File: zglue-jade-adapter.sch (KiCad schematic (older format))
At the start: 63 parts, among them J1 543630489, J2 543630489, U1 zGlue-Jade

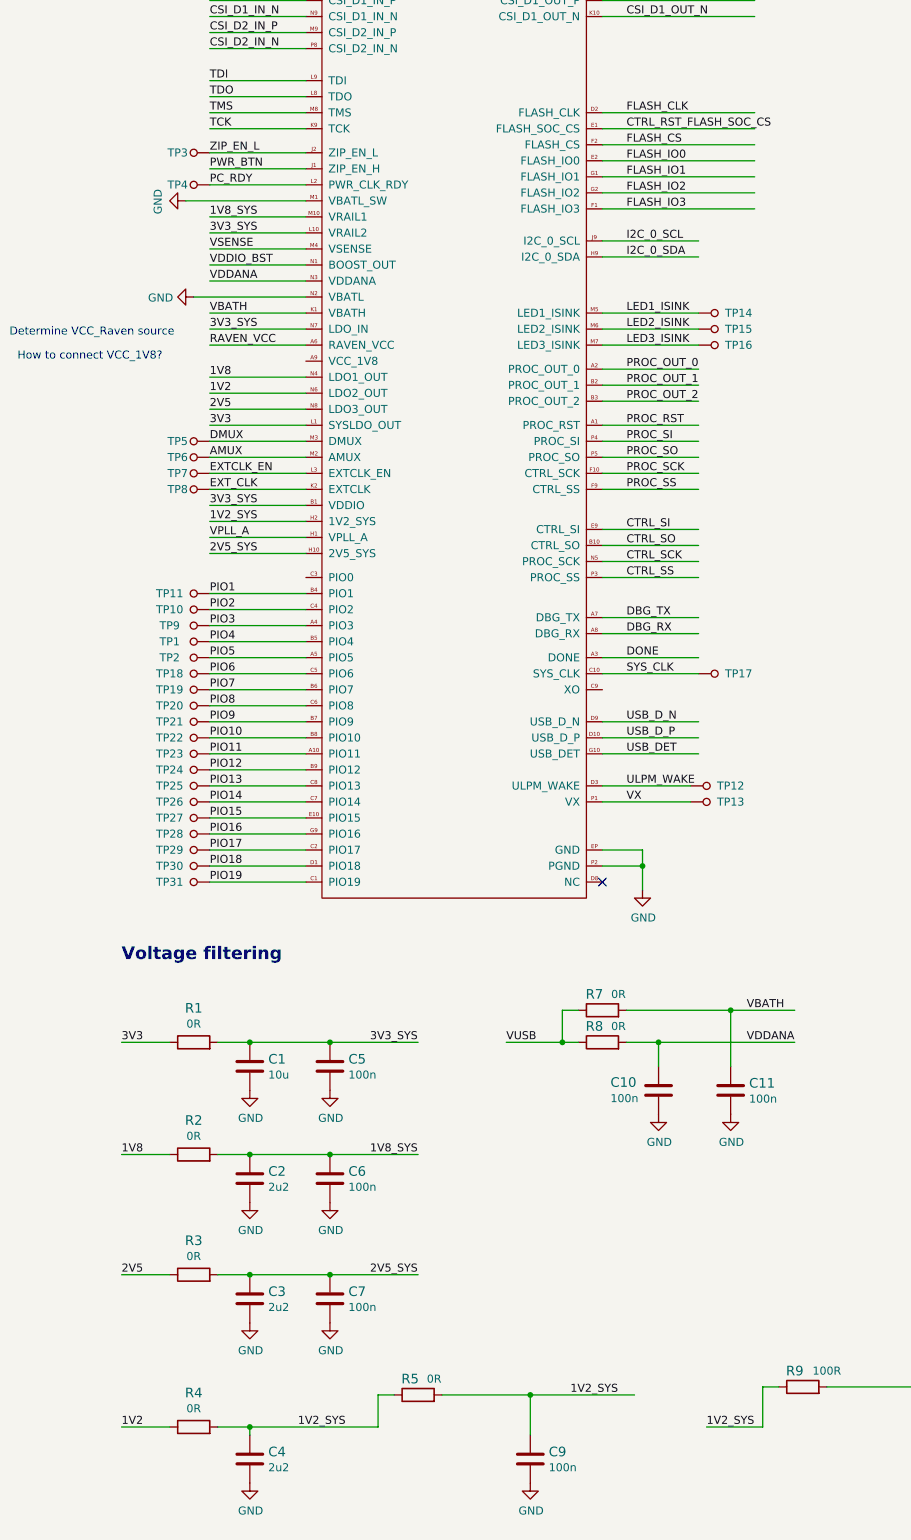
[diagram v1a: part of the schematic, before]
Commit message: Move C1,2,3,4 closer to LDOs' outputs
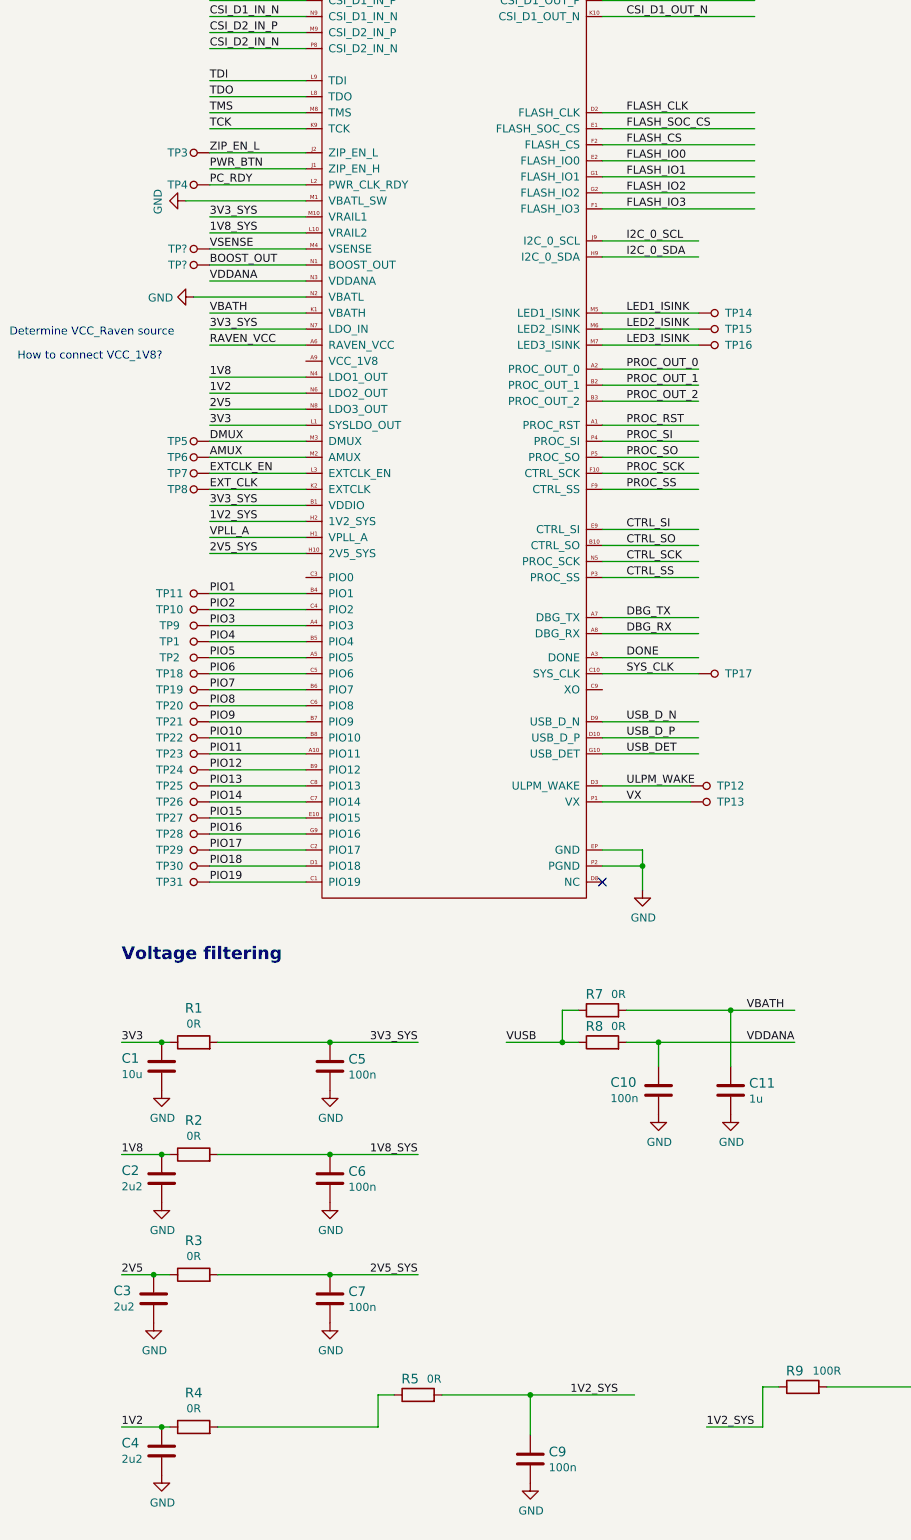
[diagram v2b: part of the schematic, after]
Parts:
- removed C11: C_100n_0402_6V3, antmicro-footprints:0402-cap, symbol antmicroCapacitors0402:C_100n_0402_6V3
- added C11: C_1u_0603, antmicro-footprints:0603-cap, symbol antmicroCapacitors0603:C_1u_0603
- added TP? (x2): TP_SMD1MM, antmicro-footprints:Testpoint_smd_1mm, symbol antmicroTestPoints:TP_SMD1MM
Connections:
- net labels added: BOOST_OUT, FLASH_SOC_CS
- net labels removed: VDDIO_BST
- wire segments 249 -> 248
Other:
- moved on the sheet: C1, C2, C3, C4
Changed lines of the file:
@@
 Wire Wire Line
 	2350 3000 1750 3000
+Text Label 1750 3000 0    50   ~ 0
+1V8_SYS
 Text Label 1750 2900 0    50   ~ 0
-1V8_SYS
-Text Label 1750 3000 0    50   ~ 0
 3V3_SYS
 Wire Wire Line
@@
 VSENSE
 Text Label 1750 3200 0    50   ~ 0
-VDDIO_BST
+BOOST_OUT
 Text Label 1750 5450 0    50   ~ 0
 PIO3
@@
 Jade chip
 $Comp
-L antmicroCapacitors0402:C_10u_0402 C1
-U 1 1 5DA0000B
-P 2000 8200
-F 0 "C1" H 2115 8245 60  0000 L CNN
-F 1 "C_10u_0402" H 2000 8050 60  0001 C CNN
-F 2 "antmicro-footprints:0402-cap" H 2200 8400 60  0001 L CNN
-F 3 "" H 2000 8200 50  0001 C CNN
-F 4 "TDK" H 2200 8600 60  0001 L CNN "Manufacturer"
-F 5 "C1005X5R0J106M050BC" H 2200 8500 60  0001 L CNN "MPN"
-F 6 "10u" H 2115 8147 50  0000 L CNN "Val"
-	1    2000 8200
-	1    0    0    -1
-$EndComp
-$Comp
 L antmicroCapacitors0402:C_100n_0402_6V3 C5
 U 1 1 5DA00317
@@
 L power:GND #PWR03
 U 1 1 5DA0044B
-P 2000 8350
-F 0 "#PWR03" H 2000 8100 50  0001 C CNN
-F 1 "GND" H 2005 8177 50  0000 C CNN
-F 2 "" H 2000 8350 50  0001 C CNN
-F 3 "" H 2000 8350 50  0001 C CNN
-	1    2000 8350
+P 1450 8350
+F 0 "#PWR03" H 1450 8100 50  0001 C CNN
+F 1 "GND" H 1455 8177 50  0000 C CNN
+F 2 "" H 1450 8350 50  0001 C CNN
+F 3 "" H 1450 8350 50  0001 C CNN
+	1    1450 8350
 	1    0    0    -1
 $EndComp
@@
 $EndComp
 Wire Wire Line
-	1800 8050 2000 8050
-Connection ~ 2000 8050
-Wire Wire Line
-	2000 8050 2500 8050
-Wire Wire Line
 	2500 8050 3050 8050
 Connection ~ 2500 8050
 Wire Wire Line
-	1500 8050 1200 8050
+	1500 8050 1450 8050
 Text Label 1200 8050 0    50   ~ 0
 3V3
@@
 L power:GND #PWR04
 U 1 1 5DA29CC6
-P 2000 9050
-F 0 "#PWR04" H 2000 8800 50  0001 C CNN
-F 1 "GND" H 2005 8877 50  0000 C CNN
-F 2 "" H 2000 9050 50  0001 C CNN
-F 3 "" H 2000 9050 50  0001 C CNN
-	1    2000 9050
+P 1450 9050
+F 0 "#PWR04" H 1450 8800 50  0001 C CNN
+F 1 "GND" H 1455 8877 50  0000 C CNN
+F 2 "" H 1450 9050 50  0001 C CNN
+F 3 "" H 1450 9050 50  0001 C CNN
+	1    1450 9050
 	1    0    0    -1
 $EndComp
@@
 Connection ~ 2500 8750
 Wire Wire Line
-	1500 8750 1200 8750
-Wire Wire Line
-	1800 8750 2000 8750
+	1500 8750 1450 8750
 $Comp
 L antmicroCapacitors0402:C_2u2_0402 C2
 U 1 1 5DA30683
-P 2000 8900
-F 0 "C2" H 2115 8945 60  0000 L CNN
-F 1 "C_2u2_0402" H 2000 8750 60  0001 C CNN
-F 2 "antmicro-footprints:0402-cap" H 2200 9100 60  0001 L CNN
-F 3 "" H 2000 8900 50  0001 C CNN
-F 4 "TDK" H 2200 9300 60  0001 L CNN "Manufacturer"
-F 5 "C1005X5R1A225K050BC" H 2200 9200 60  0001 L CNN "MPN"
-F 6 "2u2" H 2115 8847 50  0000 L CNN "Val"
-	1    2000 8900
-	1    0    0    -1
-$EndComp
-Connection ~ 2000 8750
-Wire Wire Line
-	2000 8750 2500 8750
+P 1450 8900
+F 0 "C2" H 1200 8950 60  0000 L CNN
+F 1 "C_2u2_0402" H 1450 8750 60  0001 C CNN
+F 2 "antmicro-footprints:0402-cap" H 1650 9100 60  0001 L CNN
+F 3 "" H 1450 8900 50  0001 C CNN
+F 4 "TDK" H 1650 9300 60  0001 L CNN "Manufacturer"
+F 5 "C1005X5R1A225K050BC" H 1650 9200 60  0001 L CNN "MPN"
+F 6 "2u2" H 1200 8850 50  0000 L CNN "Val"
+	1    1450 8900
+	1    0    0    -1
+$EndComp
 $Comp
 L power:GND #PWR06
 U 1 1 5DA307EF
-P 2000 10800
-F 0 "#PWR06" H 2000 10550 50  0001 C CNN
-F 1 "GND" H 2005 10627 50  0000 C CNN
-F 2 "" H 2000 10800 50  0001 C CNN
-F 3 "" H 2000 10800 50  0001 C CNN
-	1    2000 10800
+P 1450 10750
+F 0 "#PWR06" H 1450 10500 50  0001 C CNN
+F 1 "GND" H 1455 10577 50  0000 C CNN
+F 2 "" H 1450 10750 50  0001 C CNN
+F 3 "" H 1450 10750 50  0001 C CNN
+	1    1450 10750
 	1    0    0    -1
 $EndComp
@@
 $EndComp
 Wire Wire Line
-	1500 10450 1200 10450
-Wire Wire Line
-	1800 10450 2000 10450
-Connection ~ 2000 10450
+	1500 10450 1450 10450
 $Comp
 L antmicroCapacitors0402:C_2u2_0402 C4
 U 1 1 5DA3080C
-P 2000 10650
-F 0 "C4" H 2115 10695 60  0000 L CNN
-F 1 "C_2u2_0402" H 2000 10500 60  0001 C CNN
-F 2 "antmicro-footprints:0402-cap" H 2200 10850 60  0001 L CNN
-F 3 "" H 2000 10650 50  0001 C CNN
-F 4 "TDK" H 2200 11050 60  0001 L CNN "Manufacturer"
-F 5 "C1005X5R1A225K050BC" H 2200 10950 60  0001 L CNN "MPN"
-F 6 "2u2" H 2115 10597 50  0000 L CNN "Val"
-	1    2000 10650
+P 1450 10600
+F 0 "C4" H 1200 10650 60  0000 L CNN
+F 1 "C_2u2_0402" H 1450 10450 60  0001 C CNN
+F 2 "antmicro-footprints:0402-cap" H 1650 10800 60  0001 L CNN
+F 3 "" H 1450 10600 50  0001 C CNN
+F 4 "TDK" H 1650 11000 60  0001 L CNN "Manufacturer"
+F 5 "C1005X5R1A225K050BC" H 1650 10900 60  0001 L CNN "MPN"
+F 6 "2u2" H 1200 10550 50  0000 L CNN "Val"
+	1    1450 10600
 	1    0    0    -1
 $EndComp
@@
 Wire Wire Line
 	2800 10250 2800 10450
-Text Label 2300 10450 0    50   ~ 0
-1V2_SYS
-Wire Wire Line
-	2000 10450 2800 10450
-Wire Wire Line
-	2000 10500 2000 10450
 Wire Wire Line
 	2900 10250 2800 10250
@@
 L power:GND #PWR05
 U 1 1 5DB84A7E
-P 2000 9800
-F 0 "#PWR05" H 2000 9550 50  0001 C CNN
-F 1 "GND" H 2005 9627 50  0000 C CNN
-F 2 "" H 2000 9800 50  0001 C CNN
-F 3 "" H 2000 9800 50  0001 C CNN
-	1    2000 9800
+P 1400 9800
+F 0 "#PWR05" H 1400 9550 50  0001 C CNN
+F 1 "GND" H 1405 9627 50  0000 C CNN
+F 2 "" H 1400 9800 50  0001 C CNN
+F 3 "" H 1400 9800 50  0001 C CNN
+	1    1400 9800
 	1    0    0    -1
 $EndComp
@@
 Wire Wire Line
 	2500 9500 3050 9500
-Connection ~ 2500 9500
-Wire Wire Line
-	1500 9500 1200 9500
-Wire Wire Line
-	1800 9500 2000 9500
+Wire Wire Line
+	1500 9500 1400 9500
 $Comp
 L antmicroCapacitors0402:C_2u2_0402 C3
 U 1 1 5DB84A9B
-P 2000 9650
-F 0 "C3" H 2115 9695 60  0000 L CNN
-F 1 "C_2u2_0402" H 2000 9500 60  0001 C CNN
-F 2 "antmicro-footprints:0402-cap" H 2200 9850 60  0001 L CNN
-F 3 "" H 2000 9650 50  0001 C CNN
-F 4 "TDK" H 2200 10050 60  0001 L CNN "Manufacturer"
-F 5 "C1005X5R1A225K050BC" H 2200 9950 60  0001 L CNN "MPN"
-F 6 "2u2" H 2115 9597 50  0000 L CNN "Val"
-	1    2000 9650
-	1    0    0    -1
-$EndComp
-Connection ~ 2000 9500
-Wire Wire Line
-	2000 9500 2500 9500
+P 1400 9650
+F 0 "C3" H 1150 9700 60  0000 L CNN
+F 1 "C_2u2_0402" H 1400 9500 60  0001 C CNN
+F 2 "antmicro-footprints:0402-cap" H 1600 9850 60  0001 L CNN
+F 3 "" H 1400 9650 50  0001 C CNN
+F 4 "TDK" H 1600 10050 60  0001 L CNN "Manufacturer"
+F 5 "C1005X5R1A225K050BC" H 1600 9950 60  0001 L CNN "MPN"
+F 6 "2u2" H 1150 9600 50  0000 L CNN "Val"
+	1    1400 9650
+	1    0    0    -1
+$EndComp
 $Comp
 L power:GND #PWR014
@@
 Text Label 3600 8050 0    50   ~ 0
 VUSB
-$Comp
-L antmicroCapacitors0402:C_100n_0402_6V3 C11
-U 1 1 5DBBCE74
-P 5000 8350
-F 0 "C11" H 5115 8395 60  0000 L CNN
-F 1 "C_100n_0402_6V3" H 5000 8200 60  0001 C CNN
-F 2 "antmicro-footprints:0402-cap" H 5200 8550 60  0001 L CNN
-F 3 "" H 5000 8350 50  0001 C CNN
-F 4 "Walsin" H 5200 8750 60  0001 L CNN "Manufacturer"
-F 5 "0402X104K6R3CT" H 5200 8650 60  0001 L CNN "MPN"
-F 6 "100n" H 5115 8297 50  0000 L CNN "Val"
-	1    5000 8350
-	1    0    0    -1
-$EndComp
 $Comp
 L antmicroResistors0402:R_0R_0402 R7
@@
 FLASH_IO3
 Text Label 4350 2350 0    50   ~ 0
-CTRL_RST_FLASH_SOC_CS
+FLASH_SOC_CS
 Text Label 10850 2850 0    50   ~ 0
 FLASH_CLK
@@
 Text Notes 11550 5000 0    50   ~ 0
 LP_D1_OUT and CSI_INT are missing on LGA pinout!
+Connection ~ 1450 10450
+Wire Wire Line
+	1450 10450 1200 10450
+Wire Wire Line
+	1800 10450 2800 10450
+$Comp
+L antmicroCapacitors0402:C_10u_0402 C1
+U 1 1 5DA0000B
+P 1450 8200
+F 0 "C1" H 1200 8250 60  0000 L CNN
+F 1 "C_10u_0402" H 1450 8050 60  0001 C CNN
+F 2 "antmicro-footprints:0402-cap" H 1650 8400 60  0001 L CNN
+F 3 "" H 1450 8200 50  0001 C CNN
+F 4 "TDK" H 1650 8600 60  0001 L CNN "Manufacturer"
+F 5 "C1005X5R0J106M050BC" H 1650 8500 60  0001 L CNN "MPN"
+F 6 "10u" H 1200 8150 50  0000 L CNN "Val"
+	1    1450 8200
+	1    0    0    -1
+$EndComp
+Connection ~ 1450 8050
+Wire Wire Line
+	1450 8050 1200 8050
+Wire Wire Line
+	1800 8050 2500 8050
+Connection ~ 1450 8750
+Wire Wire Line
+	1450 8750 1200 8750
+Wire Wire Line
+	1800 8750 2500 8750
+Connection ~ 1400 9500
+Wire Wire Line
+	1400 9500 1200 9500
+Connection ~ 2500 9500
+Wire Wire Line
+	1800 9500 2500 9500
+$Comp
+L antmicroCapacitors0603:C_1u_0603 C11
+U 1 1 5DB7F637
+P 5000 8350
+F 0 "C11" H 5115 8395 60  0000 L CNN
+F 1 "C_1u_0603" H 5000 8200 60  0001 C CNN
+F 2 "antmicro-footprints:0603-cap" H 5200 8550 60  0001 L CNN
+F 3 "" H 5000 8350 50  0001 C CNN
+F 4 "WALSIN" H 5200 8750 60  0001 L CNN "Manufacturer"
+F 5 "0603X105K160CT" H 5200 8650 60  0001 L CNN "MPN"
+F 6 "1u" H 5115 8297 50  0000 L CNN "Val"
+	1    5000 8350
+	1    0    0    -1
+$EndComp
+$Comp
+L antmicroTestPoints:TP_SMD1MM TP?
+U 1 1 5DB4B7D6
+P 1650 3200
+F 0 "TP?" V 1650 3100 50  0000 C CNN
+F 1 "TP_SMD1MM" H 1650 3100 50  0001 C CNN
+F 2 "antmicro-footprints:Testpoint_smd_1mm" H 1850 3400 60  0001 L CNN
+F 3 "" H 1850 3500 60  0001 L CNN
+	1    1650 3200
+	0    1    1    0
+$EndComp
+$Comp
+L antmicroTestPoints:TP_SMD1MM TP?
+U 1 1 5DB4B87C
+P 1650 3100
+F 0 "TP?" V 1650 3000 50  0000 C CNN
+F 1 "TP_SMD1MM" H 1650 3000 50  0001 C CNN
+F 2 "antmicro-footprints:Testpoint_smd_1mm" H 1850 3300 60  0001 L CNN
+F 3 "" H 1850 3400 60  0001 L CNN
+	1    1650 3100
+	0    1    1    0
+$EndComp
 $EndSCHEMATC

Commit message: Add initial layout
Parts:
- added TP34: TP_SMD1MM, antmicro-footprints:Testpoint_smd_1mm, symbol antmicroTestPoints:TP_SMD1MM
- gave numbers to parts that had none: 2
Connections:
- net labels removed: FLASH_SOC_CS
- wire segments 248 -> 249
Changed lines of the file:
@@
 Text Label 4350 2850 0    50   ~ 0
 FLASH_IO3
-Text Label 4350 2350 0    50   ~ 0
-FLASH_SOC_CS
 Text Label 10850 2850 0    50   ~ 0
 FLASH_CLK
@@
 $EndComp
 $Comp
-L antmicroTestPoints:TP_SMD1MM TP?
+L antmicroTestPoints:TP_SMD1MM TP33
 U 1 1 5DB4B7D6
 P 1650 3200
-F 0 "TP?" V 1650 3100 50  0000 C CNN
+F 0 "TP33" V 1650 3100 50  0000 C CNN
 F 1 "TP_SMD1MM" H 1650 3100 50  0001 C CNN
 F 2 "antmicro-footprints:Testpoint_smd_1mm" H 1850 3400 60  0001 L CNN
@@
 $EndComp
 $Comp
-L antmicroTestPoints:TP_SMD1MM TP?
+L antmicroTestPoints:TP_SMD1MM TP32
 U 1 1 5DB4B87C
 P 1650 3100
-F 0 "TP?" V 1650 3000 50  0000 C CNN
+F 0 "TP32" V 1650 3000 50  0000 C CNN
 F 1 "TP_SMD1MM" H 1650 3000 50  0001 C CNN
 F 2 "antmicro-footprints:Testpoint_smd_1mm" H 1850 3300 60  0001 L CNN
@@
 	0    1    1    0
 $EndComp
+$Comp
+L antmicroTestPoints:TP_SMD1MM TP34
+U 1 1 5DB51D00
+P 4900 5850
+F 0 "TP34" V 4900 5700 50  0000 C CNN
+F 1 "TP_SMD1MM" H 4900 5750 50  0001 C CNN
+F 2 "antmicro-footprints:Testpoint_smd_1mm" H 5100 6050 60  0001 L CNN
+F 3 "" H 5100 6150 60  0001 L CNN
+	1    4900 5850
+	0    -1   -1   0
+$EndComp
+Wire Wire Line
+	4200 5850 4800 5850
+Text Label 4350 2350 0    50   ~ 0
+CTRL_RST_FLASH_SOC_CS
 $EndSCHEMATC
